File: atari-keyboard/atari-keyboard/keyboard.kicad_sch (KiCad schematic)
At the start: 210 parts, among them SW201 ESC, SW202 1, SW203 2, SW204 3, SW205 4, SW206 5, SW207 6, SW208 7, SW209 8, SW210 9, SW211 0, SW212 LT, SW213 GT, SW214 BS, SW215 C_UP, SW216 C_LEFT, SW217 C_DOWN, SW218 C_RIGHT, SW219 TAB, SW220 Q, SW221 W, SW222 E, SW223 R, SW224 T, SW225 Y, SW226 U, SW227 I, SW228 O, SW229 P, SW230 DASH, SW231 EQUAL, SW232 RET, SW233 HELP, SW234 RESET, SW235 OPTION, SW236 SELECT, SW237 CTRL, SW238 A, SW239 S, SW240 D, SW241 F, SW242 G, SW243 H, SW244 J, SW245 K, SW246 L, SW247 SEMI, SW248 PLUS, SW249 ASTRIX, SW250 CAPS, SW251 START, SW252 POWER, SW253 MENU, SW254 TURBO, SW255 FN, SW256 LSHIFT, SW257 Z, SW258 X, SW259 C, SW260 V, SW261 B, SW262 N, SW263 M, SW264 COMMA, SW265 PERIOD, SW266 SLASH, SW267 RSHIFT, SW268 INV, SW269 BREAK, SW270 SPACE

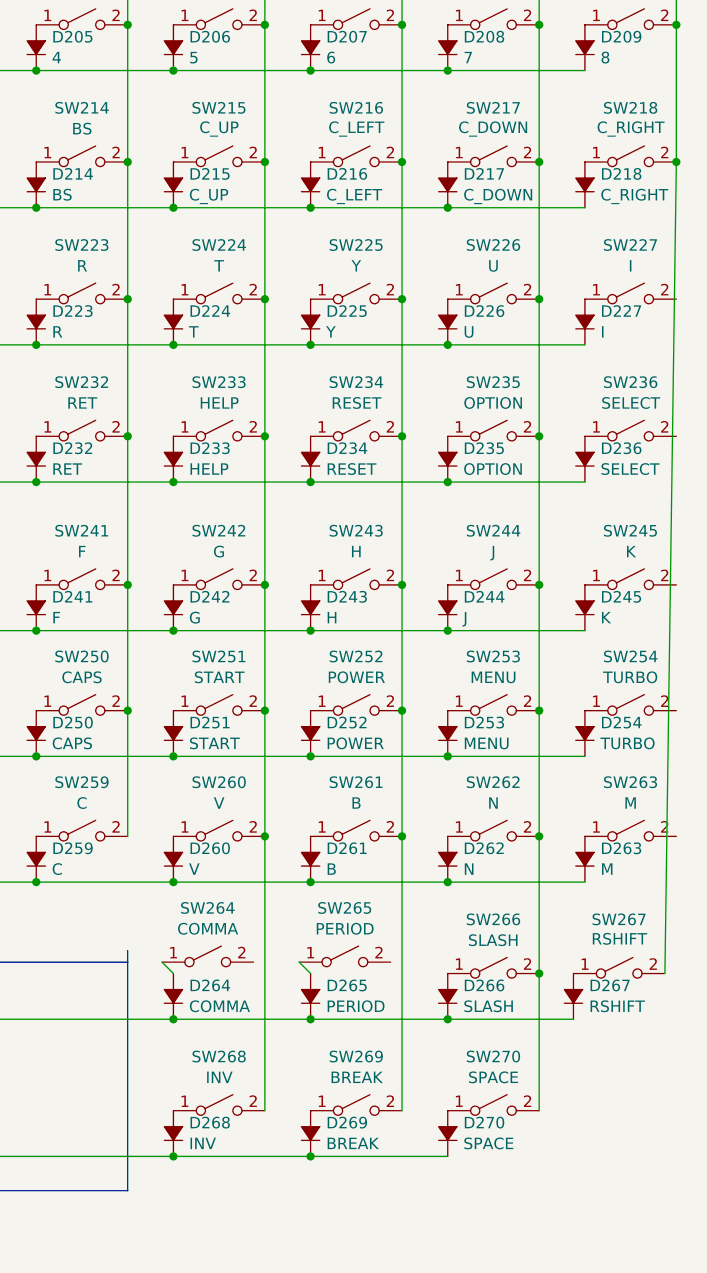
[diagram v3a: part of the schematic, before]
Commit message: Discovered some of the schematic grid was out of alignment
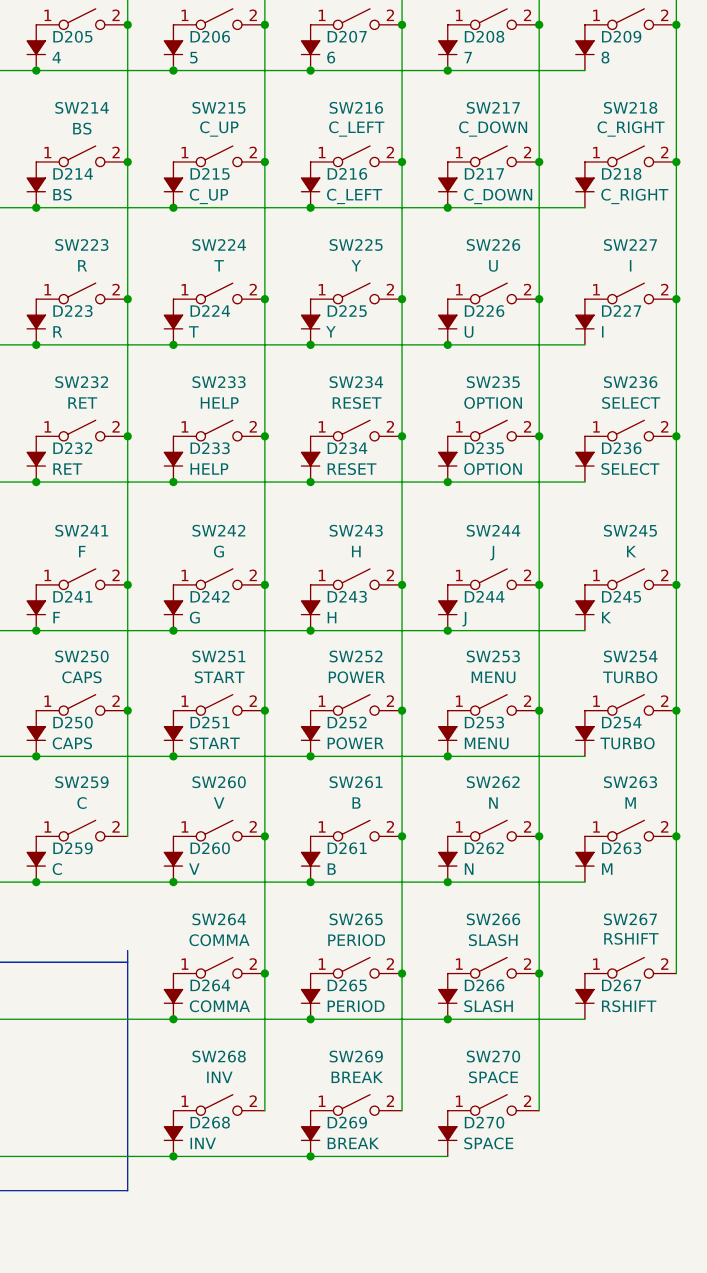
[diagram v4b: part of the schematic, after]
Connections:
- net C6: now also SW264.2 (B)
- net C7: now also SW265.2 (B)
- net C9: now also SW227.2 (B), SW236.2 (B), SW245.2 (B), SW254.2 (B), SW263.2 (B)
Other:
- moved on the sheet: D267, SW264, SW265, SW267
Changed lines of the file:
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@@
   (junction (at 184.15 41.91) (diameter 0) (color 0 0 0 0)
   )
+  (junction (at 270.51 67.31) (diameter 0) (color 0 0 0 0)
+  )
   (junction (at 184.15 104.14) (diameter 0) (color 0 0 0 0)
   )
@@
   (junction (at 168.91 41.91) (diameter 0) (color 0 0 0 0)
   )
+  (junction (at 270.51 127) (diameter 0) (color 0 0 0 0)
+  )
   (junction (at 194.31 82.55) (diameter 0) (color 0 0 0 0)
   )
@@
   (junction (at 184.15 132.08) (diameter 0) (color 0 0 0 0)
   )
-  (junction (at 270.51 52.07) (diameter 0) (color 0 0 0 0)
-  )
   (junction (at 153.67 104.14) (diameter 0) (color 0 0 0 0)
   )
@@
   (junction (at 153.67 118.11) (diameter 0) (color 0 0 0 0)
   )
+  (junction (at 270.51 99.06) (diameter 0) (color 0 0 0 0)
+  )
   (junction (at 148.59 36.83) (diameter 0) (color 0 0 0 0)
   )
@@
   (junction (at 224.79 113.03) (diameter 0) (color 0 0 0 0)
   )
+  (junction (at 240.03 142.24) (diameter 0) (color 0 0 0 0)
+  )
+  (junction (at 270.51 82.55) (diameter 0) (color 0 0 0 0)
+  )
   (junction (at 199.39 104.14) (diameter 0) (color 0 0 0 0)
   )
@@
   (junction (at 194.31 52.07) (diameter 0) (color 0 0 0 0)
   )
+  (junction (at 270.51 52.07) (diameter 0) (color 0 0 0 0)
+  )
   (junction (at 179.07 52.07) (diameter 0) (color 0 0 0 0)
   )
@@
   (junction (at 229.87 104.14) (diameter 0) (color 0 0 0 0)
   )
+  (junction (at 224.79 142.24) (diameter 0) (color 0 0 0 0)
+  )
   (junction (at 245.11 147.32) (diameter 0) (color 0 0 0 0)
   )
@@
   (junction (at 199.39 57.15) (diameter 0) (color 0 0 0 0)
   )
+  (junction (at 270.51 113.03) (diameter 0) (color 0 0 0 0)
+  )
   (junction (at 179.07 113.03) (diameter 0) (color 0 0 0 0)
   )
@@
     (stroke (width 0) (type default) (color 0 0 0 0))
   )
+  (wire (pts (xy 270.51 67.31) (xy 270.51 82.55))
+    (stroke (width 0) (type default) (color 0 0 0 0))
+  )
+  (wire (pts (xy 224.79 142.24) (xy 224.79 157.48))
+    (stroke (width 0) (type default) (color 0 0 0 0))
+  )
   (wire (pts (xy 209.55 113.03) (xy 209.55 127))
     (stroke (width 0) (type default) (color 0 0 0 0))
@@
     (stroke (width 0) (type default) (color 0 0 0 0))
   )
+  (wire (pts (xy 270.51 127) (xy 270.51 142.24))
+    (stroke (width 0) (type default) (color 0 0 0 0))
+  )
   (wire (pts (xy 245.11 87.63) (xy 260.35 87.63))
     (stroke (width 0) (type default) (color 0 0 0 0))
@@
     (stroke (width 0) (type default) (color 0 0 0 0))
   )
-  (wire (pts (xy 224.79 127) (xy 224.79 157.48))
+  (wire (pts (xy 224.79 127) (xy 224.79 142.24))
     (stroke (width 0) (type default) (color 0 0 0 0))
   )
@@
     (stroke (width 0) (type default) (color 0 0 0 0))
   )
+  (wire (pts (xy 270.51 82.55) (xy 270.51 99.06))
+    (stroke (width 0) (type default) (color 0 0 0 0))
+  )
   (wire (pts (xy 148.59 52.07) (xy 148.59 67.31))
     (stroke (width 0) (type default) (color 0 0 0 0))
@@
     (stroke (width 0) (type default) (color 0 0 0 0))
   )
-  (wire (pts (xy 228.6 140.97) (xy 229.87 142.24))
+  (wire (pts (xy 270.51 52.07) (xy 270.51 67.31))
     (stroke (width 0) (type default) (color 0 0 0 0))
   )
@@
     (stroke (width 0) (type default) (color 0 0 0 0))
   )
-  (wire (pts (xy 240.03 127) (xy 240.03 157.48))
+  (wire (pts (xy 240.03 127) (xy 240.03 142.24))
     (stroke (width 0) (type default) (color 0 0 0 0))
   )
@@
     (stroke (width 0) (type default) (color 0 0 0 0))
   )
-  (wire (pts (xy 245.11 147.32) (xy 259.08 147.32))
+  (wire (pts (xy 245.11 147.32) (xy 260.35 147.32))
     (stroke (width 0) (type default) (color 0 0 0 0))
   )
@@
     (stroke (width 0) (type default) (color 0 0 0 0))
   )
-  (wire (pts (xy 213.36 140.97) (xy 214.63 142.24))
-    (stroke (width 0) (type default) (color 0 0 0 0))
-  )
   (wire (pts (xy 199.39 57.15) (xy 214.63 57.15))
     (stroke (width 0) (type default) (color 0 0 0 0))
@@
     (stroke (width 0) (type default) (color 0 0 0 0))
   )
-  (wire (pts (xy 270.51 52.07) (xy 269.24 142.24))
+  (wire (pts (xy 153.67 57.15) (xy 168.91 57.15))
     (stroke (width 0) (type default) (color 0 0 0 0))
   )
-  (wire (pts (xy 153.67 57.15) (xy 168.91 57.15))
+  (wire (pts (xy 240.03 142.24) (xy 240.03 157.48))
     (stroke (width 0) (type default) (color 0 0 0 0))
   )
@@
     (stroke (width 0) (type default) (color 0 0 0 0))
   )
+  (wire (pts (xy 270.51 113.03) (xy 270.51 127))
+    (stroke (width 0) (type default) (color 0 0 0 0))
+  )
   (wire (pts (xy 214.63 57.15) (xy 229.87 57.15))
     (stroke (width 0) (type default) (color 0 0 0 0))
@@
     (stroke (width 0) (type default) (color 0 0 0 0))
   )
+  (wire (pts (xy 270.51 99.06) (xy 270.51 113.03))
+    (stroke (width 0) (type default) (color 0 0 0 0))
+  )
   (wire (pts (xy 125.73 57.15) (xy 138.43 57.15))
     (stroke (width 0) (type default) (color 0 0 0 0))
@@
     (pin "2")
   )
-  (symbol (lib_id "Switch:SW_SPST") (at 264.16 142.24 0) (unit 1)
+  (symbol (lib_id "Switch:SW_SPST") (at 265.43 142.24 0) (unit 1)
     (in_bom yes) (on_board yes)
-    (property "Reference" "SW267" (id 0) (at 264.16 136.271 0))
-    (property "Value" "RSHIFT" (id 1) (at 264.16 138.43 0))
-    (property "Footprint" "Button_Switch_Keyboard:SW_Cherry_MX_1.75u_PCB" (id 2) (at 264.16 142.24 0)
+    (property "Reference" "SW267" (id 0) (at 265.43 136.271 0))
+    (property "Value" "RSHIFT" (id 1) (at 265.43 138.43 0))
+    (property "Footprint" "Button_Switch_Keyboard:SW_Cherry_MX_1.75u_PCB" (id 2) (at 265.43 142.24 0)
       (effects (font (size 1.27 1.27)) hide)
     )
-    (property "Datasheet" "~" (id 3) (at 264.16 142.24 0)
+    (property "Datasheet" "~" (id 3) (at 265.43 142.24 0)
       (effects (font (size 1.27 1.27)) hide)
     )
@@
     )
   )
-  (symbol (lib_id "Switch:SW_SPST") (at 233.68 140.97 0) (unit 1)
+  (symbol (lib_id "Switch:SW_SPST") (at 234.95 142.24 0) (unit 1)
     (in_bom yes) (on_board yes)
-    (property "Reference" "SW265" (id 0) (at 233.68 135.001 0))
-    (property "Value" "PERIOD" (id 1) (at 233.68 137.3124 0))
-    (property "Footprint" "Button_Switch_Keyboard:SW_Cherry_MX_1.00u_PCB" (id 2) (at 233.68 140.97 0)
+    (property "Reference" "SW265" (id 0) (at 234.95 136.271 0))
+    (property "Value" "PERIOD" (id 1) (at 234.95 138.5824 0))
+    (property "Footprint" "Button_Switch_Keyboard:SW_Cherry_MX_1.00u_PCB" (id 2) (at 234.95 142.24 0)
       (effects (font (size 1.27 1.27)) hide)
     )
-    (property "Datasheet" "~" (id 3) (at 233.68 140.97 0)
+    (property "Datasheet" "~" (id 3) (at 234.95 142.24 0)
       (effects (font (size 1.27 1.27)) hide)
     )
@@
     )
   )
-  (symbol (lib_id "atari-keyboard-rescue:D_Small_ALT-Device") (at 259.08 144.78 90) (unit 1)
+  (symbol (lib_id "atari-keyboard-rescue:D_Small_ALT-Device") (at 260.35 144.78 90) (unit 1)
     (in_bom yes) (on_board yes)
-    (property "Reference" "D267" (id 0) (at 260.8072 143.6116 90)
+    (property "Reference" "D267" (id 0) (at 262.0772 143.6116 90)
       (effects (font (size 1.27 1.27)) (justify right))
     )
-    (property "Value" "RSHIFT" (id 1) (at 260.8072 145.923 90)
+    (property "Value" "RSHIFT" (id 1) (at 262.0772 145.923 90)
       (effects (font (size 1.27 1.27)) (justify right))
     )
-    (property "Footprint" "retro-kbd:Diode-dual" (id 2) (at 259.08 144.78 90)
+    (property "Footprint" "retro-kbd:Diode-dual" (id 2) (at 260.35 144.78 90)
       (effects (font (size 1.27 1.27)) hide)
     )
-    (property "Datasheet" "~" (id 3) (at 259.08 144.78 90)
+    (property "Datasheet" "~" (id 3) (at 260.35 144.78 90)
       (effects (font (size 1.27 1.27)) hide)
     )
@@
     )
   )
-  (symbol (lib_id "Switch:SW_SPST") (at 218.44 140.97 0) (unit 1)
+  (symbol (lib_id "Switch:SW_SPST") (at 219.71 142.24 0) (unit 1)
     (in_bom yes) (on_board yes)
-    (property "Reference" "SW264" (id 0) (at 218.44 135.001 0))
-    (property "Value" "COMMA" (id 1) (at 218.44 137.3124 0))
-    (property "Footprint" "Button_Switch_Keyboard:SW_Cherry_MX_1.00u_PCB" (id 2) (at 218.44 140.97 0)
+    (property "Reference" "SW264" (id 0) (at 219.71 136.271 0))
+    (property "Value" "COMMA" (id 1) (at 219.71 138.5824 0))
+    (property "Footprint" "Button_Switch_Keyboard:SW_Cherry_MX_1.00u_PCB" (id 2) (at 219.71 142.24 0)
       (effects (font (size 1.27 1.27)) hide)
     )
-    (property "Datasheet" "~" (id 3) (at 218.44 140.97 0)
+    (property "Datasheet" "~" (id 3) (at 219.71 142.24 0)
       (effects (font (size 1.27 1.27)) hide)
     )
